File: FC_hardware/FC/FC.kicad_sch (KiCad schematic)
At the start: 16 parts, among them U1 MP2348, U2 AMS1117-3.3

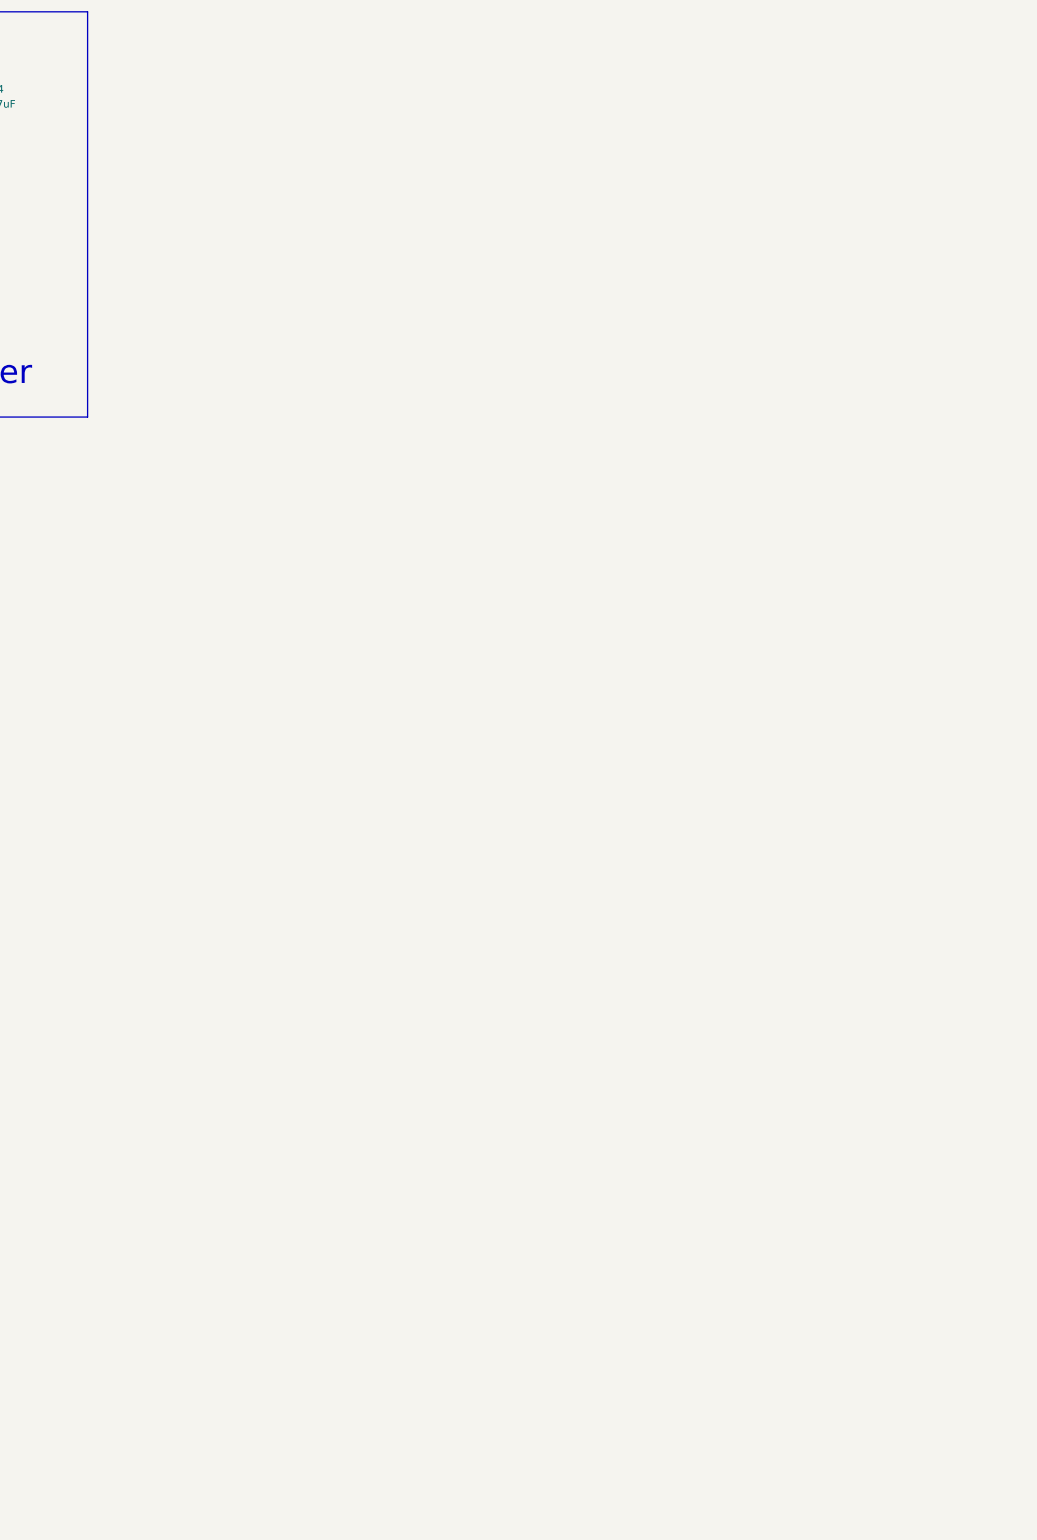
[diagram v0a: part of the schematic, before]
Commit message: STM pin config added
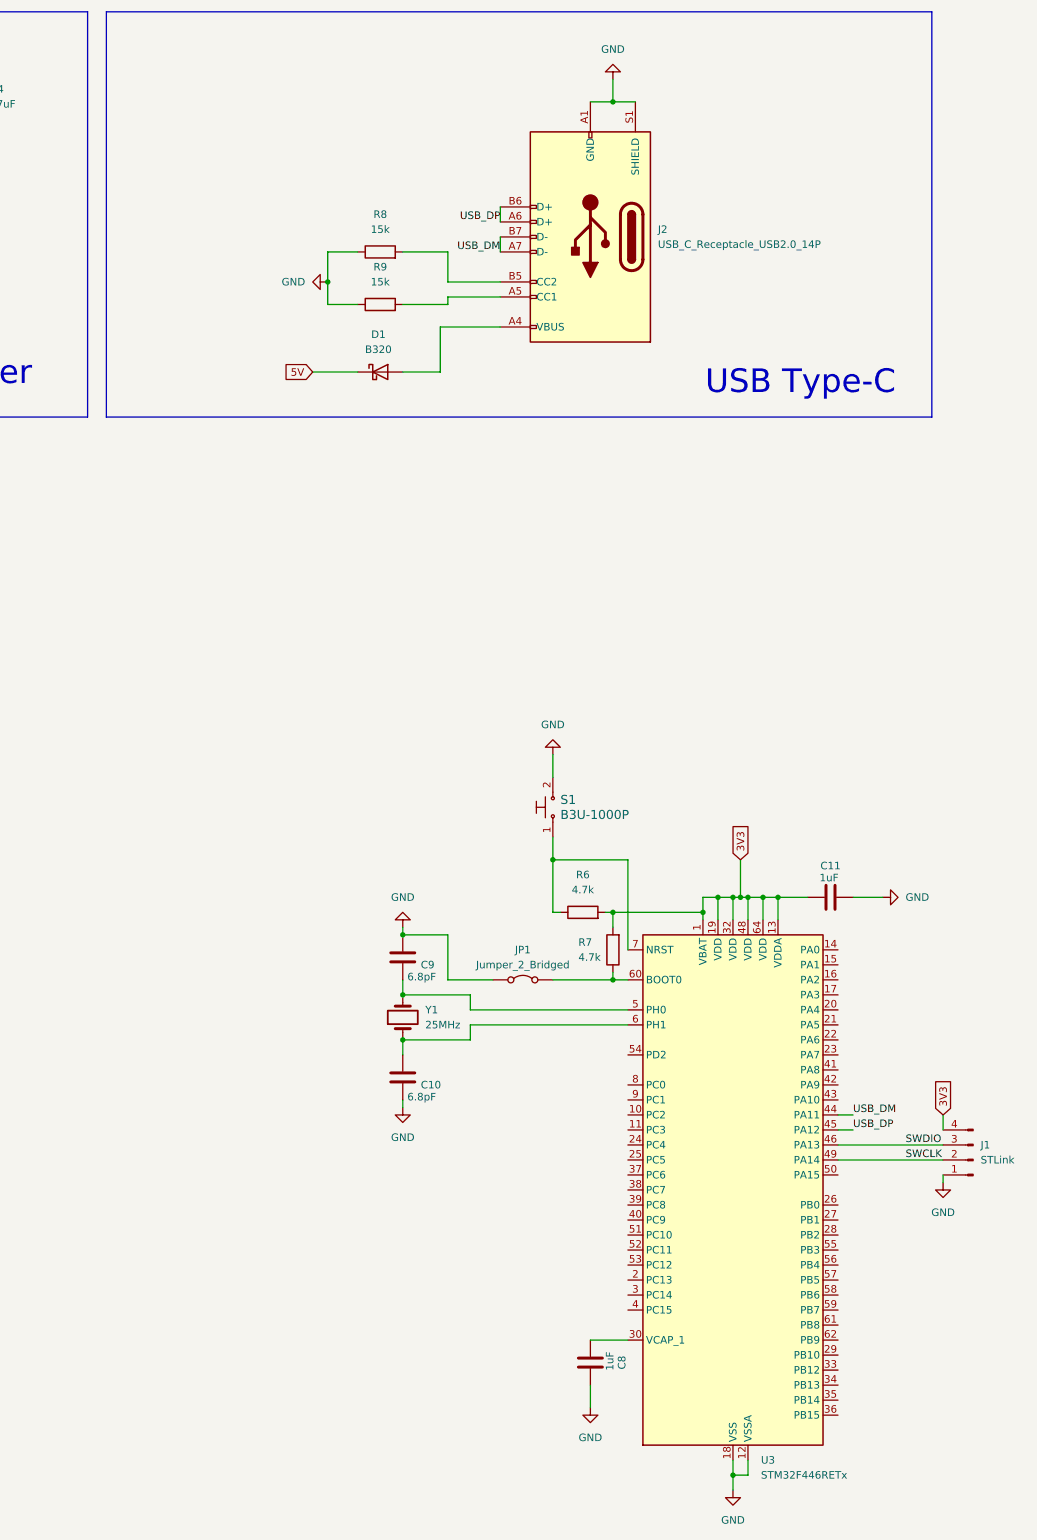
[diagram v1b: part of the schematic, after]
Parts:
- added C10, C9: 6.8pF, Capacitor_SMD:C_0201_0603Metric, symbol Device:C
- added C11, C8: 1uF, Capacitor_SMD:C_0805_2012Metric, symbol Device:C
- added D1: B320, Diode_SMD:D_SMC, symbol Diode:B320
- added J1: STLink, symbol Connector:Conn_01x04_Pin
- added J2: USB_C_Receptacle_USB2.0_14P, symbol Connector:USB_C_Receptacle_USB2.0_14P
- added JP1: Jumper_2_Bridged, symbol Jumper:Jumper_2_Bridged
- added R6, R7: 4.7k, Resistor_SMD:R_0201_0603Metric, symbol Device:R
- added R8, R9: 15k, Resistor_SMD:R_0201_0603Metric, symbol Device:R
- added S1: B3U-1000P, digikey-footprints:Switch_Tactile_SMD_B3U-1000P, symbol dk_Tactile-Switches:B3U-1000P
- added U3: STM32F446RETx, Package_QFP:LQFP-64_10x10mm_P0.5mm, symbol MCU_ST_STM32F4:STM32F446RETx
- added Y1: 25MHz, symbol Device:Crystal
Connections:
- net 3V3: now also C11.2, J1.4 (Pin_4), R6.2, R7.2, U3.1 (VBAT), U3.13 (VDDA), U3.19 (VDD), U3.32 (VDD), U3.48 (VDD), U3.64 (VDD)
- net 5V: now also D1.1 (K)
- net GND: now also C10.2, C11.1, C8.1, C9.1, J1.1 (Pin_1), J2.A1 (GND), J2.A12 (GND), J2.B1 (GND), J2.B12 (GND), J2.S1 (SHIELD), JP1.1 (A), R8.1, R9.1, S1.2, U3.12 (VSSA), U3.18 (VSS), U3.31 (VSS), U3.47 (VSS), U3.63 (VSS)
- new net: R6.1, S1.1, U3.7 (NRST)
- new net: C8.2, U3.30 (VCAP_1)
- new net: C10.1, U3.6 (PH1), Y1.1
- new net: C9.2, U3.5 (PH0), Y1.2
- new net: D1.2 (A), J2.A4 (VBUS), J2.A9 (VBUS), J2.B4 (VBUS), J2.B9 (VBUS)
- new net: J2.A5 (CC1), R9.2
- new net: J2.B5 (CC2), R8.2
- new net: JP1.2 (B), R7.1, U3.60 (BOOT0)
- new net SWCLK: J1.2 (Pin_2), U3.49 (PA14)
- new net SWDIO: J1.3 (Pin_3), U3.46 (PA13)
- new net USB_DM: J2.A7 (D-), J2.B7 (D-), U3.44 (PA11)
- new net USB_DP: J2.A6 (D+), J2.B6 (D+), U3.45 (PA12)
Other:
- note added: "USB Type-C"

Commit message: schematic things...
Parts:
- added C12, C13, C14, C15, C16, C17: 0.1uF, Capacitor_SMD:C_0603_1608Metric, symbol Device:C
- added J3: S8B-ZR_LF__SN_, footprints:JST_S8B-ZR_LF__SN_, symbol S8B-ZR_LF__SN_:S8B-ZR_LF__SN_
- added JP2: ESC_TEL, symbol Jumper:Jumper_2_Small_Open
- added R10: 1k, Resistor_SMD:R_0201_0603Metric, symbol Device:R
- added R11: 4.7k, Resistor_SMD:R_0201_0603Metric, symbol Device:R
- added R12: 40.2k, Resistor_SMD:R_0201_0603Metric, symbol Device:R
- added U4: MPU-9250, Sensor_Motion:InvenSense_QFN-24_3x3mm_P0.4mm, symbol Sensor_Motion:MPU-9250
- added U5: DPS368XTSA1, footprints:XDCR_DPS368XTSA1, symbol DPS368XTSA1:DPS368XTSA1
- added U6: Ai-Thinker-Ra-02, RF_Module:Ai-Thinker-Ra-01-LoRa, symbol RF_Module:Ai-Thinker-Ra-02
- C11: value 1uF -> 0.1uF; footprint Capacitor_SMD:C_0805_2012Metric -> Capacitor_SMD:C_0603_1608Metric
- JP1: value Jumper_2_Bridged -> BOOT0
- R8, R9: value 15k -> 5.1k
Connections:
- net 3V3: now also C12.1, C14.1, C15.1, U4.1 (RESV_VDDIO), U4.13 (VDD), U4.8 (VDDIO), U5.6 (VDDIO), U5.8 (VDD), U6.3 (VDD)
- net BAT: now also J3.7 (VCC), R12.1
- net GND: now also C12.2, C13.2, C14.2, C15.2, C16.2, C17.2, J3.8 (GND), R11.1, U4.11 (FSYNC), U4.18 (GND), U4.20 (RESV_GND), U4.22 (~{CS}), U5.1 (GND), U5.7 (GND), U6.1 (GND), U6.16 (GND), U6.2 (GND), U6.9 (GND)
- net ADC_I: now reaches U3.10 (PC2)
- net ADC_I: now also C16.1, R10.1
- net BAR_CSB: now reaches U3.2 (PC13)
- net BAR_CSB: now also U5.2 (CSB)
- net LORA_NSS: now reaches U3.20 (PA4)
- net LORA_NSS: now also U6.15 (~{NSS})
- net LORA_RST: now reaches U3.21 (PA5)
- net LORA_RST: now also U6.4 (~{RESET})
- net ESC_1: now reaches U3.22 (PA6)
- net ESC_1: now also J3.6 (S1)
- net ESC_2: now reaches U3.23 (PA7)
- net ESC_2: now also J3.5 (S2)
- net LORA_IRQN: now reaches U3.24 (PC4)
- net LORA_IRQN: now also U6.5 (DIO0)
- net at U3.25 (PC5): now also JP2.2 (B)
- net ESC_3: now reaches U3.26 (PB0)
- net ESC_3: now also J3.4 (S3)
- net ESC_4: now reaches U3.27 (PB1)
- net ESC_4: now also J3.3 (S4)
- net LORA_BAR_SCK: now reaches U3.34 (PB13)
- net LORA_BAR_SCK: now also U5.4 (SCK), U6.12 (SCK)
- net LORA_BAR_MISO: now reaches U3.35 (PB14)
- net LORA_BAR_MISO: now also U5.5 (SDO), U6.13 (MISO)
- net LORA_BAR_MOSI: now reaches U3.36 (PB15)
- net LORA_BAR_MOSI: now also U5.3 (SDI), U6.14 (MOSI)
- net IMU_IRQN: now reaches U3.54 (PD2)
- net IMU_IRQN: now also U4.12 (INT)
- net IMU_SCK: now reaches U3.55 (PB3)
- net IMU_SCK: now also U4.23 (SCL/SCLK)
- net IMU_MISO: now reaches U3.56 (PB4)
- net IMU_MISO: now also U4.9 (AD0/MISO)
- net IMU_MOSI: now reaches U3.57 (PB5)
- net IMU_MOSI: now also U4.24 (SDA/MOSI)
- net ADC_U: now reaches U3.9 (PC1)
- net ADC_U: now also C17.1, R11.2, R12.2
- new net: C13.1, U4.10 (REGOUT)
- new net: J3.2 (CURR), R10.2
- new net ESC_RX: J3.1 (TEL), JP2.1 (A)
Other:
- note added: "ESC_PWR"
- note added: "IMU"
- note added: "LoRa/Barometer"
- moved on the sheet: C10, C11, C8, C9, JP1, R6, R7, S1, U3, Y1

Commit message: schematic is done
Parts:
- removed J1: STLink, symbol Connector:Conn_01x04_Pin
- removed J2: USB_C_Receptacle_USB2.0_14P, symbol Connector:USB_C_Receptacle_USB2.0_14P
- removed J3: S8B-ZR_LF__SN_, footprints:JST_S8B-ZR_LF__SN_, symbol S8B-ZR_LF__SN_:S8B-ZR_LF__SN_
- removed S1: B3U-1000P, digikey-footprints:Switch_Tactile_SMD_B3U-1000P, symbol dk_Tactile-Switches:B3U-1000P
- removed Y1: 25MHz, symbol Device:Crystal
- added D2: Power-Red, LED_SMD:LED_0805_2012Metric, symbol Device:LED_Small
- added D3: Status-Green, LED_SMD:LED_0805_2012Metric, symbol Device:LED_Small
- added J1: Pin_01x04, Connector_PinHeader_1.27mm:PinHeader_1x04_P1.27mm_Vertical, symbol Connector_Generic:Conn_01x04
- added J10, J11, J12, J9: GND, Connector_Wire:SolderWire-0.1sqmm_1x01_D0.4mm_OD1mm, symbol Connector:Conn_01x01_Pin
- added J13: Pin_02x03, Connector_PinHeader_1.27mm:PinHeader_2x03_P1.27mm_Vertical, symbol Connector_Generic:Conn_01x06
- added J14, J15: Pin_01x03, Connector_PinHeader_1.27mm:PinHeader_1x03_P1.27mm_Vertical, symbol Connector_Generic:Conn_01x03
- added J16: PB2, Connector_Wire:SolderWire-0.1sqmm_1x01_D0.4mm_OD1mm, symbol Connector:Conn_01x01_Pin
- added J17: PC9, Connector_Wire:SolderWire-0.1sqmm_1x01_D0.4mm_OD1mm, symbol Connector:Conn_01x01_Pin
- added J18: PC8, Connector_Wire:SolderWire-0.1sqmm_1x01_D0.4mm_OD1mm, symbol Connector:Conn_01x01_Pin
- added J19: PB7, Connector_Wire:SolderWire-0.1sqmm_1x01_D0.4mm_OD1mm, symbol Connector:Conn_01x01_Pin
- added J2: USB4105GFA120, footprints:GCT_USB4105GFA120, symbol USB4105GFA120:USB4105GFA120
- added J20: PB6, Connector_Wire:SolderWire-0.1sqmm_1x01_D0.4mm_OD1mm, symbol Connector:Conn_01x01_Pin
- added J21: PA8, Connector_Wire:SolderWire-0.1sqmm_1x01_D0.4mm_OD1mm, symbol Connector:Conn_01x01_Pin
- added J22: PC11, Connector_Wire:SolderWire-0.1sqmm_1x01_D0.4mm_OD1mm, symbol Connector:Conn_01x01_Pin
- added J23: PC10, Connector_Wire:SolderWire-0.1sqmm_1x01_D0.4mm_OD1mm, symbol Connector:Conn_01x01_Pin
- added J24: PC12, Connector_Wire:SolderWire-0.1sqmm_1x01_D0.4mm_OD1mm, symbol Connector:Conn_01x01_Pin
- added J25: PB10, Connector_Wire:SolderWire-0.1sqmm_1x01_D0.4mm_OD1mm, symbol Connector:Conn_01x01_Pin
- added J26: PC7, Connector_Wire:SolderWire-0.1sqmm_1x01_D0.4mm_OD1mm, symbol Connector:Conn_01x01_Pin
- added J27: PC6, Connector_Wire:SolderWire-0.1sqmm_1x01_D0.4mm_OD1mm, symbol Connector:Conn_01x01_Pin
- added J3: 530480810, footprints:MOLEX_530480810, symbol 530480810:530480810
- added J4: BAT, Connector_Wire:SolderWire-0.1sqmm_1x01_D0.4mm_OD1mm, symbol Connector:Conn_01x01_Pin
- added J5, J6: 5V, Connector_Wire:SolderWire-0.1sqmm_1x01_D0.4mm_OD1mm, symbol Connector:Conn_01x01_Pin
- added J7, J8: 3V3, Connector_Wire:SolderWire-0.1sqmm_1x01_D0.4mm_OD1mm, symbol Connector:Conn_01x01_Pin
- added Q1: BC807W, Package_TO_SOT_SMD:SOT-323_SC-70, symbol Transistor_BJT:BC807W
- added R13, R14, R17, R18: 1k, Resistor_SMD:R_0201_0603Metric, symbol Device:R
- added R15, R16: 4.7k, Resistor_SMD:R_0201_0603Metric, symbol Device:R
- added S1: EVQ-P7L01P, footprints:SW_EVQ-P7L01P, symbol EVQ-P7L01P:EVQ-P7L01P
- added Y1: ABM8G-25MHZ, footprints:XTAL_ABM8G-25.000MHZ-4Y-T3, symbol ABM8G-25.000MHZ-4Y-T3:ABM8G-25.000MHZ-4Y-T3
- JP1: footprint (none) -> Jumper:SolderJumper-2_P1.3mm_Bridged_RoundedPad1.0x1.5mm
- JP2: footprint (none) -> Jumper:SolderJumper-2_P1.3mm_Open_RoundedPad1.0x1.5mm
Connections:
- net 3V3: now also D2.2 (A), J1.4 (3V3), J7.1 (Pin_1), J8.1 (Pin_1), Q1.2 (E), R15.2, R16.2
- net 5V: now also J13.2 (5V), J14.2 (5V), J5.1 (Pin_1), J6.1 (Pin_1)
- net BAT: now also J3.7 (VCC), J4.1 (Pin_1)
- net ESC_1: now also J3.6 (S1)
- net ESC_2: now also J3.5 (S2)
- net ESC_3: now also J3.4 (S3)
- net ESC_4: now also J3.3 (S4)
- net ESC_RX: now also J3.1 (TEL)
- net GND: now also R8.2, J1.1 (GND), J10.1 (Pin_1), J11.1 (Pin_1), J12.1 (Pin_1), J13.1 (GND), J14.1 (GND), J15.1 (GND), J2.A1_B12 (GND), J2.B1_A12 (GND), J2.SH1 (SHELL_GND), J2.SH2 (SHELL_GND), J2.SH3 (SHELL_GND), J2.SH4 (SHELL_GND), J3.8 (GND), J9.1 (Pin_1), R13.1, R14.1, R18.1, S1.2_1, S1.2_2, Y1.2 (GND), Y1.4 (GND); no longer R8.1
- net SWCLK: now also J1.2 (CLK)
- net SWDIO: now also J1.3 (DIO)
- net USB_DM: now also J2.A7 (DN1), J2.B7 (DN2)
- net USB_DP: now also J2.A6 (DP1), J2.B6 (DP2)
- net at R6.1, U3.7 (NRST): now also S1.1_1, S1.1_2
- net at C10.1, U3.6 (PH1): now also Y1.3
- net at C9.2, U3.5 (PH0): now also Y1.1
- net at D1.2 (A): now also J2.A4_B9 (VBUS), J2.B4_A9 (VBUS)
- net at R9.2: now also J2.A5 (CC1)
- net SBUS_RX: now reaches U3.15 (PA1)
- net SBUS_RX: now also Q1.3 (C), R18.2
- net GPS_TX: now reaches U3.16 (PA2)
- net GPS_TX: now also J13.4 (TX)
- net GPS_RX: now reaches U3.17 (PA3)
- net GPS_RX: now also J13.3 (RX)
- net GEN_MOSI: now reaches U3.28 (PB2)
- net GEN_MOSI: now also J16.1 (Pin_1)
- net GEN_SCL: now reaches U3.29 (PB10)
- net GEN_SCL: now also J25.1 (Pin_1)
- net at U3.33 (PB12): now also D3.2 (A)
- net GEN_TX: now reaches U3.37 (PC6)
- net GEN_TX: now also J27.1 (Pin_1)
- net GEN_RX: now reaches U3.38 (PC7)
- net GEN_RX: now also J26.1 (Pin_1)
- net TIM8_3: now reaches U3.39 (PC8)
- net TIM8_3: now also J18.1 (Pin_1)
- net TIM8_4: now reaches U3.40 (PC9)
- net TIM8_4: now also J17.1 (Pin_1)
- net TIM1_1: now reaches U3.41 (PA8)
- net TIM1_1: now also J21.1 (Pin_1)
- net DEBUG_TX: now reaches U3.42 (PA9)
- net DEBUG_TX: now also J15.2 (TX)
- net DEBUG_RX: now reaches U3.43 (PA10)
- net DEBUG_RX: now also J15.3 (RX)
- net GEN_SCK: now reaches U3.51 (PC10)
- net GEN_SCK: now also J23.1 (Pin_1)
- net GEN_MISO: now reaches U3.52 (PC11)
- net GEN_MISO: now also J22.1 (Pin_1)
- net GEN_SDA: now reaches U3.53 (PC12)
- net GEN_SDA: now also J24.1 (Pin_1)
- net TIM4_1: now reaches U3.58 (PB6)
- net TIM4_1: now also J20.1 (Pin_1)
- net TIM4_2: now reaches U3.59 (PB7)
- net TIM4_2: now also J19.1 (Pin_1)
- net MAG_SCL: now reaches U3.61 (PB8)
- net MAG_SCL: now also J13.5 (SCL), R16.1
- net MAG_SDA: now reaches U3.62 (PB9)
- net MAG_SDA: now also J13.6 (SDA), R15.1
- net at R10.2: now also J3.2 (CURR)
- new net: Q1.1 (B), R17.1
- new net: J14.3 (SBUS), R17.2
- new net: J2.B5 (CC2), R8.1
- new net: D2.1 (K), R13.2
- new net: D3.1 (K), R14.2
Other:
- note added: "CONNECTORS"
- note added: "GPS/SBUS"
- company: (none) -> Lego
- title: (none) -> Drone FC
- moved on the sheet: C10, C12, C13, C16, C17, D1, JP2, R10, R11, R12, R8, R9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
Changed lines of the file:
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@@
 	(generator_version "8.0")
 	(paper "A2")
+	(title_block
+		(title "Drone FC")
+		(date "2024-09-01")
+		(company "Lego")
+	)

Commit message: footprint and PCB outline changes
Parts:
- D1: footprint Diode_SMD:D_SMC -> Diode_SMD:D_SMA
- J10, J11, J12, J16, J17, J18, J19, J20, J21, J22, J23, J24, J25, J26, J27, J4, J5, J6, J7, J8, J9: footprint Connector_Wire:SolderWire-0.1sqmm_1x01_D0.4mm_OD1mm -> footprints:1.27mm_pin
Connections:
- no-connect marks 0 -> 16

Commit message: Layout pcb
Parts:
- added C18, C19, C20, C21, C22: 0.1uF, Capacitor_SMD:C_0603_1608Metric, symbol Device:C
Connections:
- net 3V3: now also C18.2, C19.2, C20.2, C21.2, C22.2
- net GND: now also C18.1, C19.1, C20.1, C21.1, C22.1
